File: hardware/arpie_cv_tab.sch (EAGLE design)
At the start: 62 parts, among them IC1 MCP4726, IC2 MCP601OT, IC3 LM27675M5_CHARGEPUMP, IC4 LM358D, IC5 LM4041A12DBZ

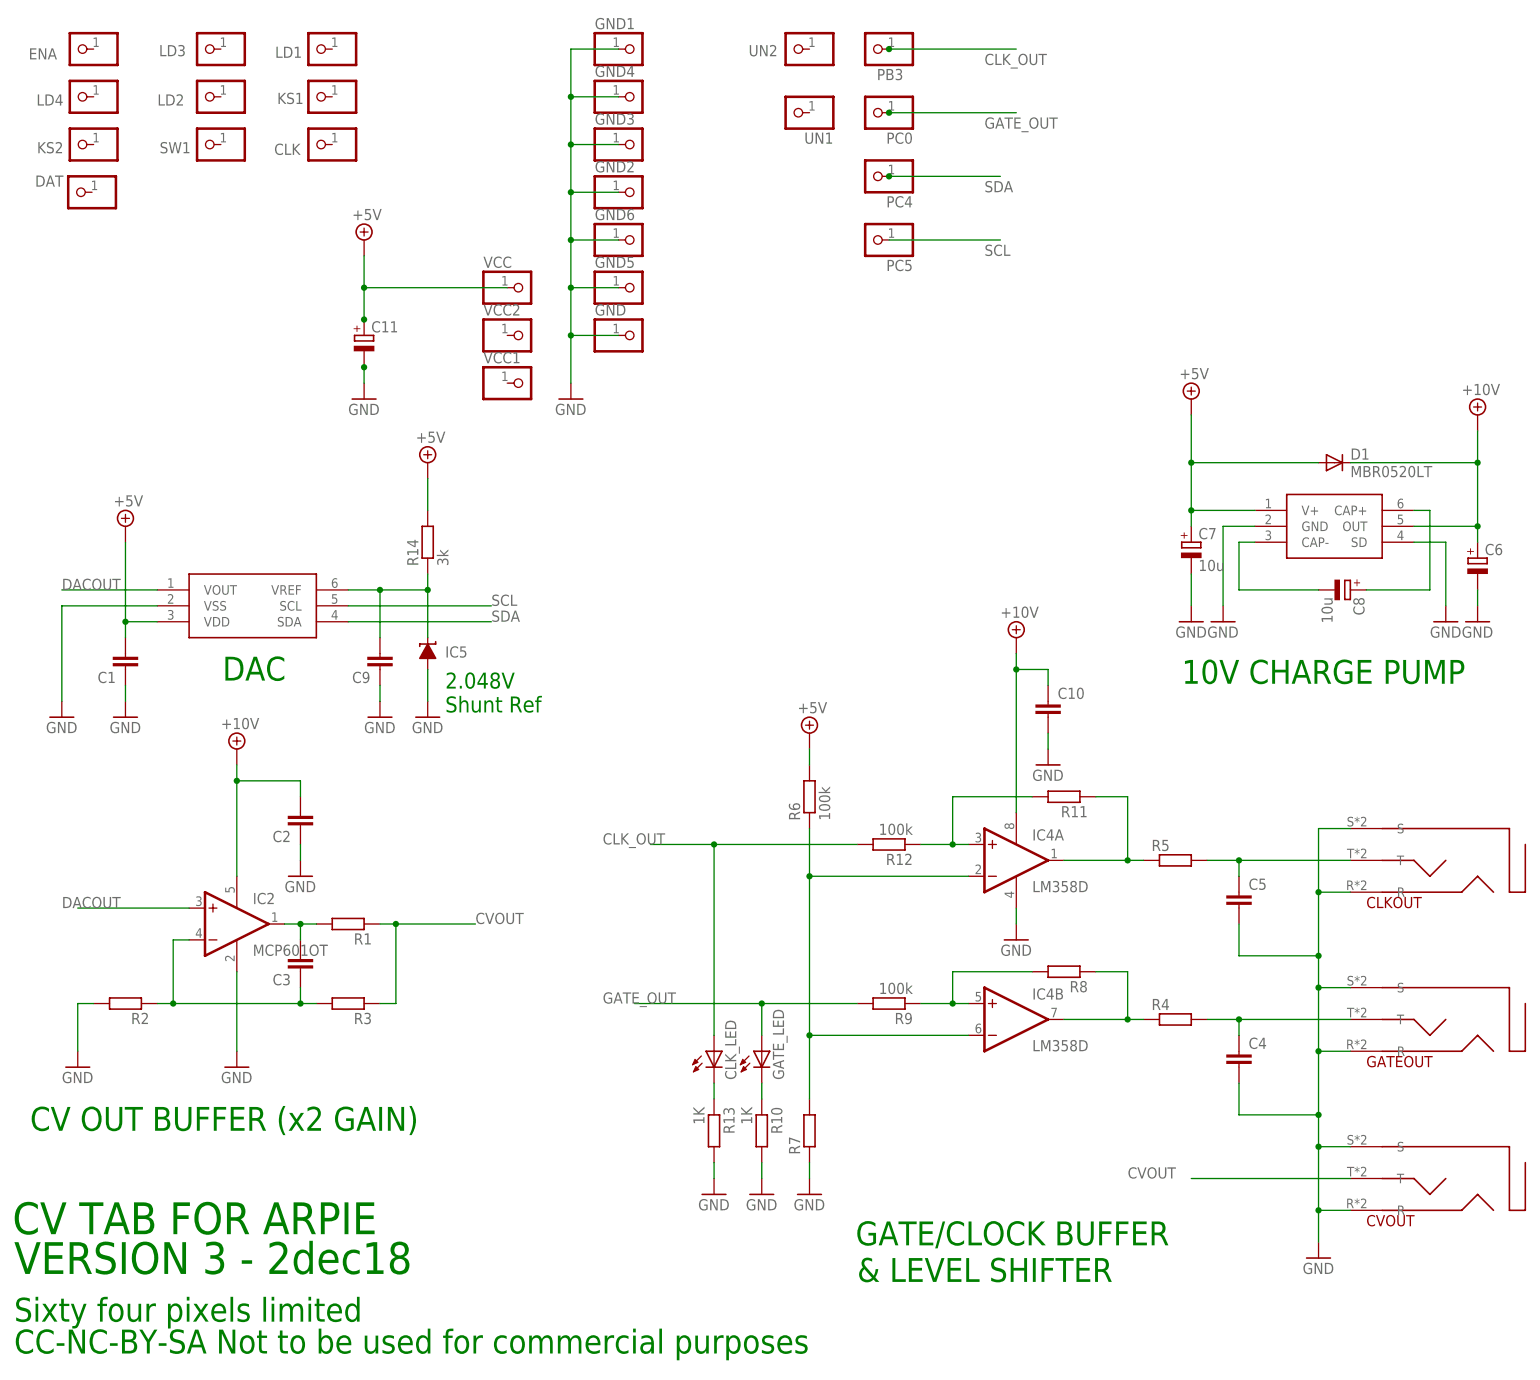
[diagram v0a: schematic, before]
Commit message: v5 added eeprom
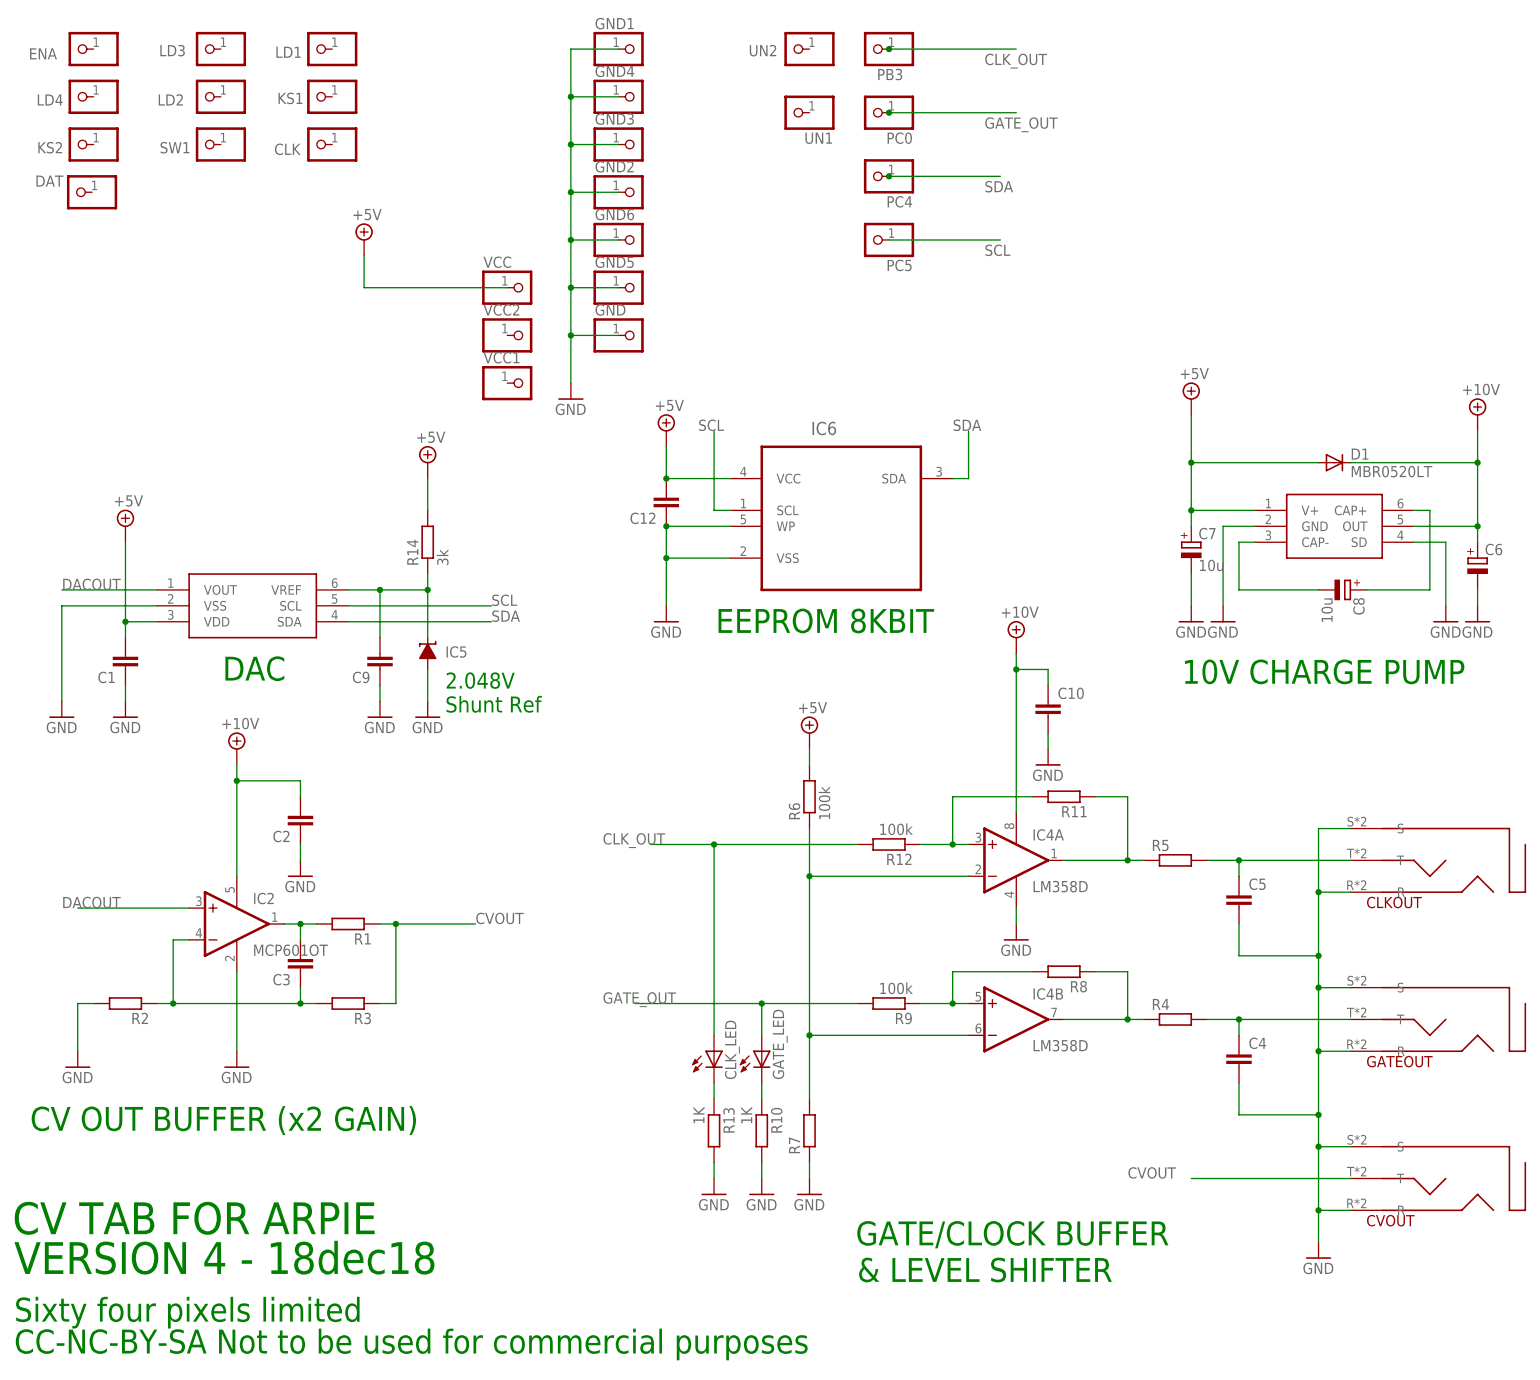
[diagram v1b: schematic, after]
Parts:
- removed C11: (no value), rcl:CPOL-EUE2.5-5
- added C12: (no value), resistor:C-EUC0805
- added IC6: 24LC_16BT-I/OT, Microchip-24LCxxx:24LC_16BT-I/OT
- CLK_LED, GATE_LED: device adafruit:LED3MM -> led:LEDCHIP-LED0805
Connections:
- net +5V: now also C12.2, IC6.VCC; no longer C11.+
- net GND: now also C12.1, IC6.VSS, IC6.WP; no longer C11.-
- net SCL: now also IC6.SCL
- net SDA: now also IC6.SDA
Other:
- note added: "EEPROM 8KBIT"
- note added: "VERSION 4 - 18dec18"
- note removed: "VERSION 3 - 2dec18"
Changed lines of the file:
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@@
 <part name="GND" library="adafruit" deviceset="PINHD-1X1" device=""/>
 <part name="VCC" library="adafruit" deviceset="PINHD-1X1" device=""/>
-<part name="CLK_LED" library="adafruit" deviceset="LED" device="3MM"/>
-<part name="GATE_LED" library="adafruit" deviceset="LED" device="3MM"/>
+<part name="CLK_LED" library="led" deviceset="LED" device="CHIP-LED0805"/>
+<part name="GATE_LED" library="led" deviceset="LED" device="CHIP-LED0805"/>
 <part name="R10" library="rcl" deviceset="R-EU_" device="R0805" value="1K"/>
 <part name="R13" library="rcl" deviceset="R-EU_" device="R0805" value="1K"/>
@@
 <part name="C9" library="resistor" deviceset="C-EU" device="C0805"/>
 <part name="GND24" library="SparkFun" deviceset="GND" device=""/>
-<part name="GND25" library="SparkFun" deviceset="GND" device=""/>
-<part name="C11" library="rcl" deviceset="CPOL-EU" device="E2.5-5"/>
+<part name="IC6" library="Microchip-24LCxxx" deviceset="24LC_" device="" technology="16BT-I/OT"/>
+<part name="SUPPLY9" library="supply2" deviceset="+5V" device=""/>
+<part name="C12" library="resistor" deviceset="C-EU" device="C0805"/>
+<part name="GND26" library="SparkFun" deviceset="GND" device=""/>
 </parts>
 <sheets>
@@
 <text x="193.04" y="19.05" size="3.81" layer="91">&amp; LEVEL SHIFTER</text>
 <text x="58.166" y="26.67" size="5.08" layer="91">CV TAB FOR ARPIE</text>
-<text x="58.42" y="20.32" size="5.08" layer="91">VERSION 3 - 2dec18</text>
+<text x="58.42" y="20.32" size="5.08" layer="91">VERSION 4 - 18dec18</text>
 <text x="58.42" y="12.7" size="3.81" layer="91">Sixty four pixels limited</text>
 <text x="58.42" y="7.62" size="3.81" layer="91">CC-NC-BY-SA Not to be used for commercial purposes</text>
 <text x="127.254" y="109.982" size="2.54" layer="91">2.048V
 Shunt Ref</text>
+<text x="170.434" y="122.682" size="3.81" layer="91">EEPROM 8KBIT</text>
 </plain>
 <instances>
@@
 <instance part="C9" gate="G$1" x="116.84" y="116.84" rot="R180"/>
 <instance part="GND24" gate="1" x="116.84" y="109.22"/>
-<instance part="GND25" gate="1" x="114.3" y="160.02"/>
-<instance part="C11" gate="G$1" x="114.3" y="170.18"/>
+<instance part="IC6" gate="A" x="172.72" y="147.32" smashed="yes">
+<attribute name="NAME" x="185.6486" y="154.2796" size="2.0828" layer="95" ratio="10" rot="SR0"/>
+</instance>
+<instance part="SUPPLY9" gate="+5V" x="162.56" y="154.94"/>
+<instance part="C12" gate="G$1" x="162.56" y="142.24" rot="R180"/>
+<instance part="GND26" gate="1" x="162.56" y="124.46"/>
 </instances>
 <busses>
@@
 </segment>
 <segment>
-<pinref part="GND25" gate="1" pin="GND"/>
-<wire x1="114.3" y1="162.56" x2="114.3" y2="165.1" width="0.1524" layer="91"/>
-<pinref part="C11" gate="G$1" pin="-"/>
-<junction x="114.3" y="165.1"/>
+<pinref part="IC6" gate="A" pin="WP"/>
+<pinref part="GND26" gate="1" pin="GND"/>
+<wire x1="172.72" y1="139.7" x2="162.56" y2="139.7" width="0.1524" layer="91"/>
+<wire x1="162.56" y1="139.7" x2="162.56" y2="134.62" width="0.1524" layer="91"/>
+<pinref part="IC6" gate="A" pin="VSS"/>
+<wire x1="162.56" y1="134.62" x2="162.56" y2="127" width="0.1524" layer="91"/>
+<wire x1="172.72" y1="134.62" x2="162.56" y2="134.62" width="0.1524" layer="91"/>
+<junction x="162.56" y="134.62"/>
+<pinref part="C12" gate="G$1" pin="1"/>
+<junction x="162.56" y="139.7"/>
 </segment>
 </net>
@@
 <wire x1="114.3" y1="177.8" x2="114.3" y2="182.88" width="0.1524" layer="91"/>
 <pinref part="SUPPLY4" gate="+5V" pin="+5V"/>
-<wire x1="114.3" y1="172.72" x2="114.3" y2="177.8" width="0.1524" layer="91"/>
-<junction x="114.3" y="177.8"/>
-<pinref part="C11" gate="G$1" pin="+"/>
-<junction x="114.3" y="172.72"/>
 </segment>
 <segment>
@@
 <wire x1="124.46" y1="142.24" x2="124.46" y2="147.32" width="0.1524" layer="91"/>
 </segment>
+<segment>
+<pinref part="IC6" gate="A" pin="VCC"/>
+<pinref part="SUPPLY9" gate="+5V" pin="+5V"/>
+<wire x1="172.72" y1="147.32" x2="162.56" y2="147.32" width="0.1524" layer="91"/>
+<wire x1="162.56" y1="147.32" x2="162.56" y2="152.4" width="0.1524" layer="91"/>
+<pinref part="C12" gate="G$1" pin="2"/>
+<junction x="162.56" y="147.32"/>
+</segment>
 </net>
 <net name="CLK_OUT" class="0">
@@
 <label x="213.36" y="182.88" size="1.778" layer="95"/>
 </segment>
+<segment>
+<pinref part="IC6" gate="A" pin="SCL"/>
+<wire x1="172.72" y1="142.24" x2="170.18" y2="142.24" width="0.1524" layer="91"/>
+<wire x1="170.18" y1="142.24" x2="170.18" y2="154.94" width="0.1524" layer="91"/>
+<label x="167.64" y="154.94" size="1.778" layer="95"/>
+</segment>
 </net>
 <net name="SDA" class="0">
@@
 <junction x="198.12" y="195.58"/>
 </segment>
-</net>
+<segment>
+<pinref part="IC6" gate="A" pin="SDA"/>
+<wire x1="208.28" y1="147.32" x2="210.82" y2="147.32" width="0.1524" layer="91"/>
+<wire x1="210.82" y1="147.32" x2="210.82" y2="154.94" width="0.1524" layer="91"/>
+<label x="208.28" y="154.94" size="1.778" layer="95"/>
+</segment>
+</net>
